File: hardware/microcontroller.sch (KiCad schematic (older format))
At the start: 13 parts, among them U6 STM32F411CEUx, Y1 12MHz

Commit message: Associate the simple parts with footprints. Some custom footprints will need to be designed.
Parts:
- C15, C21, C22, C23, C24: footprint (none) -> Capacitors_SMD:C_0603
- C16, C17, C20: footprint (none) -> Capacitors_SMD:C_0805
- C18, C19: footprint (none) -> Capacitors_SMD:C_0402
- R12: footprint (none) -> Resistors_SMD:R_0603
- U6: footprint UFQFPN48 -> Housings_DFN_QFN:QFN-48-1EP_7x7mm_Pitch0.5mm
- Y1: footprint (none) -> Crystals:Crystal_SMD_2520-4pin_2.5x2.0mm
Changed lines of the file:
@@
 F 0 "U6" H 2400 5225 50  0000 L BNN
 F 1 "STM32F411CEUx" H 9600 5225 50  0000 R BNN
-F 2 "UFQFPN48" H 9600 5175 50  0001 R TNN
+F 2 "Housings_DFN_QFN:QFN-48-1EP_7x7mm_Pitch0.5mm" H 9600 5175 50  0001 R TNN
 F 3 "" H 6000 3400 50  0001 C CNN
 	1    6000 3400
@@
 $EndComp
 $Comp
-L VDD #PWR51
+L VDD #PWR051
 U 1 1 59427B17
 P 6000 1400
-F 0 "#PWR51" H 6000 1250 50  0001 C CNN
+F 0 "#PWR051" H 6000 1250 50  0001 C CNN
 F 1 "VDD" H 6000 1550 50  0000 C CNN
 F 2 "" H 6000 1400 50  0001 C CNN
@@
 $EndComp
 $Comp
-L VDD #PWR52
+L VDD #PWR052
 U 1 1 59427B1D
 P 1850 2200
-F 0 "#PWR52" H 1850 2050 50  0001 C CNN
+F 0 "#PWR052" H 1850 2050 50  0001 C CNN
 F 1 "VDD" H 1850 2350 50  0000 C CNN
 F 2 "" H 1850 2200 50  0001 C CNN
@@
 F 0 "C17" V 1550 2350 50  0000 L CNN
 F 1 "4.7uF" V 1550 2550 50  0000 L CNN
-F 2 "" H 1500 2500 50  0001 C CNN
+F 2 "Capacitors_SMD:C_0805" H 1500 2500 50  0001 C CNN
 F 3 "" H 1500 2500 50  0001 C CNN
 	1    1500 2500
@@
 $EndComp
 $Comp
-L GND #PWR53
+L GND #PWR053
 U 1 1 59427B2A
 P 1200 2350
-F 0 "#PWR53" H 1200 2100 50  0001 C CNN
+F 0 "#PWR053" H 1200 2100 50  0001 C CNN
 F 1 "GND" V 1200 2150 50  0000 C CNN
 F 2 "" H 1200 2350 50  0001 C CNN
@@
 $EndComp
 $Comp
-L GND #PWR57
+L GND #PWR054
 U 1 1 59427B30
 P 6000 5350
-F 0 "#PWR57" H 6000 5100 50  0001 C CNN
+F 0 "#PWR054" H 6000 5100 50  0001 C CNN
 F 1 "GND" H 6000 5200 50  0000 C CNN
 F 2 "" H 6000 5350 50  0001 C CNN
@@
 F 0 "C16" V 1550 2200 50  0000 L CNN
 F 1 "1uF" V 1550 2400 50  0000 L CNN
-F 2 "" H 1500 2350 50  0001 C CNN
+F 2 "Capacitors_SMD:C_0805" H 1500 2350 50  0001 C CNN
 F 3 "" H 1500 2350 50  0001 C CNN
 	1    1500 2350
@@
 F 0 "C15" V 1550 2050 50  0000 L CNN
 F 1 "100nF" V 1550 2250 50  0000 L CNN
-F 2 "" H 1500 2200 50  0001 C CNN
+F 2 "Capacitors_SMD:C_0603" H 1500 2200 50  0001 C CNN
 F 3 "" H 1500 2200 50  0001 C CNN
 	1    1500 2200
@@
 F 0 "C21" H 4750 6550 50  0000 L CNN
 F 1 "100nF" H 4600 6750 50  0000 L CNN
-F 2 "" H 4850 6650 50  0001 C CNN
+F 2 "Capacitors_SMD:C_0603" H 4850 6650 50  0001 C CNN
 F 3 "" H 4850 6650 50  0001 C CNN
 	1    4850 6650
@@
 F 0 "C22" H 5050 6550 50  0000 L CNN
 F 1 "100nF" H 4900 6750 50  0000 L CNN
-F 2 "" H 5150 6650 50  0001 C CNN
+F 2 "Capacitors_SMD:C_0603" H 5150 6650 50  0001 C CNN
 F 3 "" H 5150 6650 50  0001 C CNN
 	1    5150 6650
@@
 F 0 "C23" H 5350 6550 50  0000 L CNN
 F 1 "100nF" H 5200 6750 50  0000 L CNN
-F 2 "" H 5450 6650 50  0001 C CNN
+F 2 "Capacitors_SMD:C_0603" H 5450 6650 50  0001 C CNN
 F 3 "" H 5450 6650 50  0001 C CNN
 	1    5450 6650
@@
 F 0 "C24" H 5650 6550 50  0000 L CNN
 F 1 "100nF" H 5500 6750 50  0000 L CNN
-F 2 "" H 5750 6650 50  0001 C CNN
+F 2 "Capacitors_SMD:C_0603" H 5750 6650 50  0001 C CNN
 F 3 "" H 5750 6650 50  0001 C CNN
 	1    5750 6650
@@
 $EndComp
 $Comp
-L GND #PWR59
+L GND #PWR055
 U 1 1 59427B60
 P 5150 6850
-F 0 "#PWR59" H 5150 6600 50  0001 C CNN
+F 0 "#PWR055" H 5150 6600 50  0001 C CNN
 F 1 "GND" H 5150 6700 50  0000 C CNN
 F 2 "" H 5150 6850 50  0001 C CNN
@@
 $EndComp
 $Comp
-L VDD #PWR58
+L VDD #PWR056
 U 1 1 59427B66
 P 5150 6450
-F 0 "#PWR58" H 5150 6300 50  0001 C CNN
+F 0 "#PWR056" H 5150 6300 50  0001 C CNN
 F 1 "VDD" H 5150 6600 50  0000 C CNN
 F 2 "" H 5150 6450 50  0001 C CNN
@@
 F 0 "C20" H 4450 6550 50  0000 L CNN
 F 1 "4.7uF" H 4300 6750 50  0000 L CNN
-F 2 "" H 4550 6650 50  0001 C CNN
+F 2 "Capacitors_SMD:C_0805" H 4550 6650 50  0001 C CNN
 F 3 "" H 4550 6650 50  0001 C CNN
 	1    4550 6650
@@
 F 0 "Y1" V 1200 2750 50  0000 L CNN
 F 1 "12MHz" V 1200 2950 50  0000 L CNN
-F 2 "" H 1350 2900 50  0001 C CNN
+F 2 "Crystals:Crystal_SMD_2520-4pin_2.5x2.0mm" H 1350 2900 50  0001 C CNN
 F 3 "" H 1350 2900 50  0001 C CNN
 	1    1350 2900
@@
 Connection ~ 1350 3100
 $Comp
-L GND #PWR55
+L GND #PWR057
 U 1 1 59427C13
 P 1150 2900
-F 0 "#PWR55" H 1150 2650 50  0001 C CNN
+F 0 "#PWR057" H 1150 2650 50  0001 C CNN
 F 1 "GND" V 1250 2850 50  0000 C CNN
 F 2 "" H 1150 2900 50  0001 C CNN
@@
 $EndComp
 $Comp
-L GND #PWR56
+L GND #PWR058
 U 1 1 59427C19
 P 1550 2900
-F 0 "#PWR56" H 1550 2650 50  0001 C CNN
+F 0 "#PWR058" H 1550 2650 50  0001 C CNN
 F 1 "GND" V 1450 2850 50  0000 C CNN
 F 2 "" H 1550 2900 50  0001 C CNN
@@
 F 0 "C19" V 1000 2950 50  0000 L CNN
 F 1 "30pF" V 1000 3150 50  0000 L CNN
-F 2 "" H 950 3100 50  0001 C CNN
+F 2 "Capacitors_SMD:C_0402" H 950 3100 50  0001 C CNN
 F 3 "" H 950 3100 50  0001 C CNN
 	1    950  3100
@@
 F 0 "C18" V 900 2550 50  0000 L CNN
 F 1 "30pF" V 900 2750 50  0000 L CNN
-F 2 "" H 950 2700 50  0001 C CNN
+F 2 "Capacitors_SMD:C_0402" H 950 2700 50  0001 C CNN
 F 3 "" H 950 2700 50  0001 C CNN
 	1    950  2700
@@
 	1050 2700 2300 2700
 $Comp
-L GND #PWR54
+L GND #PWR059
 U 1 1 59427C31
 P 800 2900
-F 0 "#PWR54" H 800 2650 50  0001 C CNN
+F 0 "#PWR059" H 800 2650 50  0001 C CNN
 F 1 "GND" V 800 2700 50  0000 C CNN
 F 2 "" H 800 2900 50  0001 C CNN
@@
 F 0 "R12" H 2130 6770 50  0000 L CNN
 F 1 "10k" H 2130 6710 50  0000 L CNN
-F 2 "" H 2100 6750 50  0001 C CNN
+F 2 "Resistors_SMD:R_0603" H 2100 6750 50  0001 C CNN
 F 3 "" H 2100 6750 50  0001 C CNN
 	1    2100 6750
@@
 $EndComp
 $Comp
-L GND #PWR60
+L GND #PWR060
 U 1 1 5942944C
 P 2100 6950
-F 0 "#PWR60" H 2100 6700 50  0001 C CNN
+F 0 "#PWR060" H 2100 6700 50  0001 C CNN
 F 1 "GND" H 2100 6800 50  0000 C CNN
 F 2 "" H 2100 6950 50  0001 C CNN

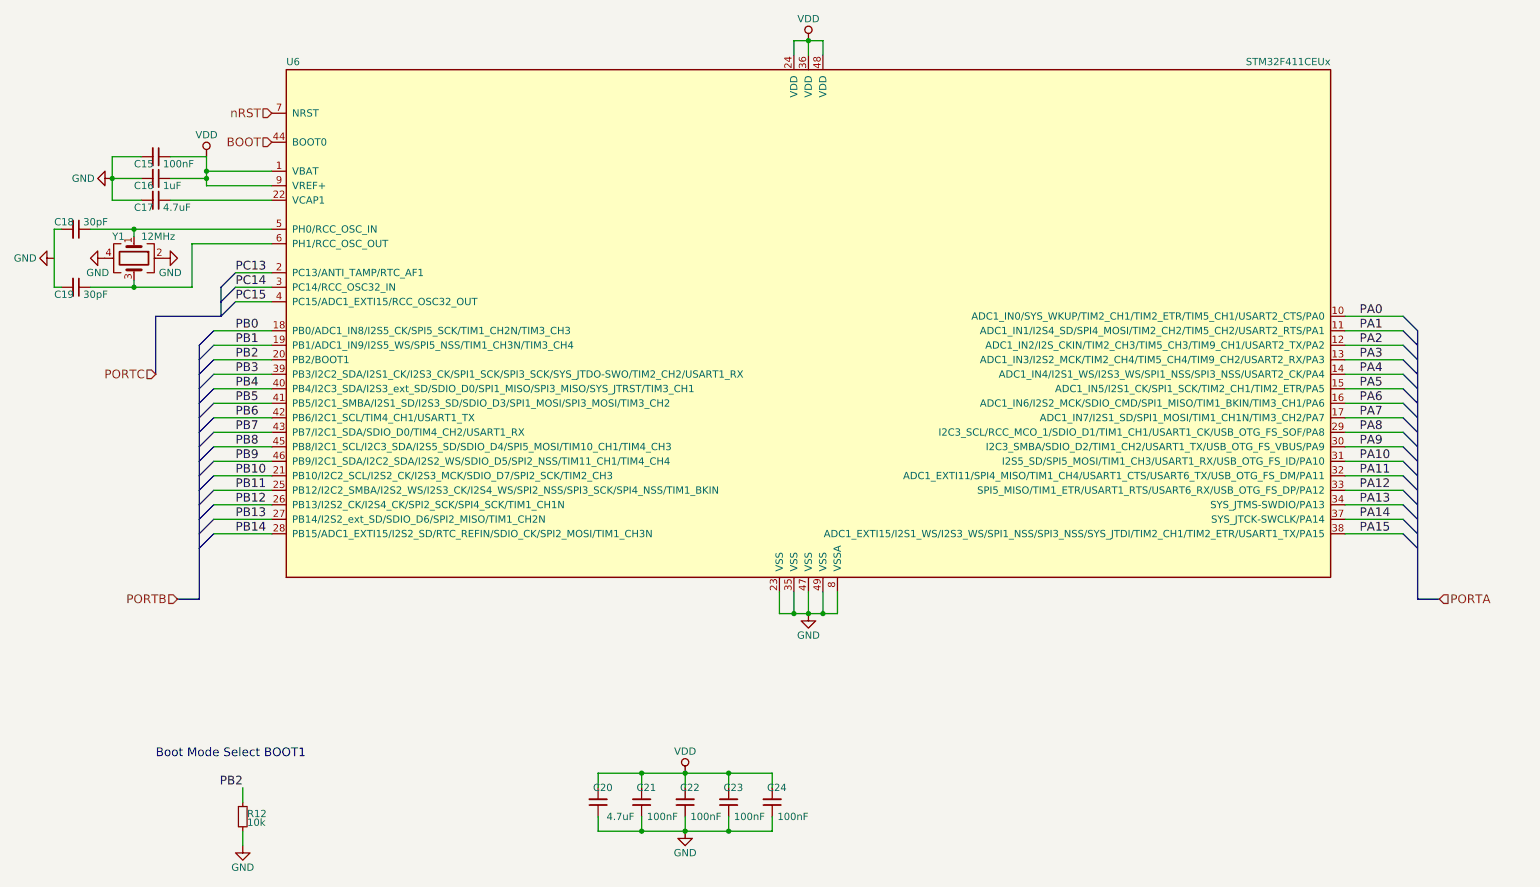
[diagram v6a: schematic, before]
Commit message: Add in some logic level translation for the camera signals. Update the annotations and plot the PDF
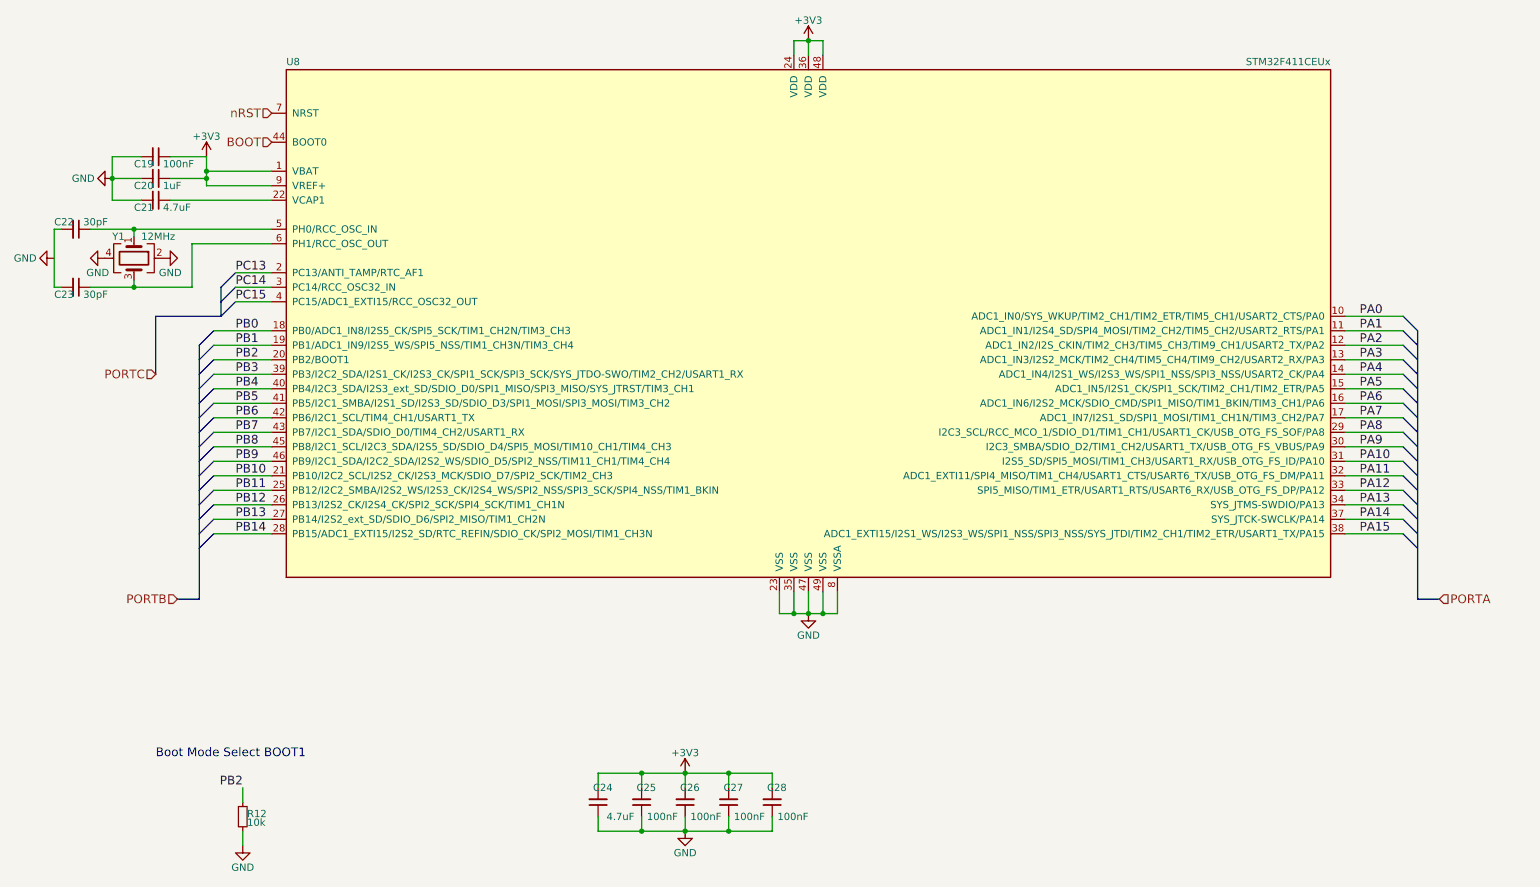
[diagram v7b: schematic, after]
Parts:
- renumbered C15 to C19, C16 to C20, C17 to C21, C18 to C22, C19 to C23, C20 to C24, C21 to C25, C22 to C26, C23 to C27, C24 to C28, U6 to U8
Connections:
- net labels added: +3V3
- net labels removed: VDD
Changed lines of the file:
@@
 P 6000 3400
 AR Path="/59427B10" Ref="U?"  Part="1"
-AR Path="/59425D39/59427B10" Ref="U6"  Part="1"
-F 0 "U6" H 2400 5225 50  0000 L BNN
+AR Path="/59425D39/59427B10" Ref="U8"  Part="1"
+F 0 "U8" H 2400 5225 50  0000 L BNN
 F 1 "STM32F411CEUx" H 9600 5225 50  0000 R BNN
 F 2 "Housings_DFN_QFN:QFN-48-1EP_7x7mm_Pitch0.5mm" H 9600 5175 50  0001 R TNN
@@
 $EndComp
 $Comp
-L VDD #PWR051
-U 1 1 59427B17
-P 6000 1400
-F 0 "#PWR051" H 6000 1250 50  0001 C CNN
-F 1 "VDD" H 6000 1550 50  0000 C CNN
-F 2 "" H 6000 1400 50  0001 C CNN
-F 3 "" H 6000 1400 50  0001 C CNN
-	1    6000 1400
-	1    0    0    -1
-$EndComp
-$Comp
-L VDD #PWR052
-U 1 1 59427B1D
-P 1850 2200
-F 0 "#PWR052" H 1850 2050 50  0001 C CNN
-F 1 "VDD" H 1850 2350 50  0000 C CNN
-F 2 "" H 1850 2200 50  0001 C CNN
-F 3 "" H 1850 2200 50  0001 C CNN
-	1    1850 2200
-	1    0    0    -1
-$EndComp
-$Comp
-L C_Small C17
+L C_Small C21
 U 1 1 59427B23
 P 1500 2500
-F 0 "C17" V 1550 2350 50  0000 L CNN
+F 0 "C21" V 1550 2350 50  0000 L CNN
 F 1 "4.7uF" V 1550 2550 50  0000 L CNN
 F 2 "Capacitors_SMD:C_0805" H 1500 2500 50  0001 C CNN
@@
 $EndComp
 $Comp
-L GND #PWR053
+L GND #PWR65
 U 1 1 59427B2A
 P 1200 2350
-F 0 "#PWR053" H 1200 2100 50  0001 C CNN
+F 0 "#PWR65" H 1200 2100 50  0001 C CNN
 F 1 "GND" V 1200 2150 50  0000 C CNN
 F 2 "" H 1200 2350 50  0001 C CNN
@@
 $EndComp
 $Comp
-L GND #PWR054
+L GND #PWR69
 U 1 1 59427B30
 P 6000 5350
-F 0 "#PWR054" H 6000 5100 50  0001 C CNN
+F 0 "#PWR69" H 6000 5100 50  0001 C CNN
 F 1 "GND" H 6000 5200 50  0000 C CNN
 F 2 "" H 6000 5350 50  0001 C CNN
@@
 $EndComp
 $Comp
-L C_Small C16
+L C_Small C20
 U 1 1 59427B36
 P 1500 2350
-F 0 "C16" V 1550 2200 50  0000 L CNN
+F 0 "C20" V 1550 2200 50  0000 L CNN
 F 1 "1uF" V 1550 2400 50  0000 L CNN
 F 2 "Capacitors_SMD:C_0805" H 1500 2350 50  0001 C CNN
@@
 $EndComp
 $Comp
-L C_Small C15
+L C_Small C19
 U 1 1 59427B3D
 P 1500 2200
-F 0 "C15" V 1550 2050 50  0000 L CNN
+F 0 "C19" V 1550 2050 50  0000 L CNN
 F 1 "100nF" V 1550 2250 50  0000 L CNN
 F 2 "Capacitors_SMD:C_0603" H 1500 2200 50  0001 C CNN
@@
 $EndComp
 $Comp
-L C_Small C21
+L C_Small C25
 U 1 1 59427B44
 P 4850 6650
-F 0 "C21" H 4750 6550 50  0000 L CNN
+F 0 "C25" H 4750 6550 50  0000 L CNN
 F 1 "100nF" H 4600 6750 50  0000 L CNN
 F 2 "Capacitors_SMD:C_0603" H 4850 6650 50  0001 C CNN
@@
 $EndComp
 $Comp
-L C_Small C22
+L C_Small C26
 U 1 1 59427B4B
 P 5150 6650
-F 0 "C22" H 5050 6550 50  0000 L CNN
+F 0 "C26" H 5050 6550 50  0000 L CNN
 F 1 "100nF" H 4900 6750 50  0000 L CNN
 F 2 "Capacitors_SMD:C_0603" H 5150 6650 50  0001 C CNN
@@
 $EndComp
 $Comp
-L C_Small C23
+L C_Small C27
 U 1 1 59427B52
 P 5450 6650
-F 0 "C23" H 5350 6550 50  0000 L CNN
+F 0 "C27" H 5350 6550 50  0000 L CNN
 F 1 "100nF" H 5200 6750 50  0000 L CNN
 F 2 "Capacitors_SMD:C_0603" H 5450 6650 50  0001 C CNN
@@
 $EndComp
 $Comp
-L C_Small C24
+L C_Small C28
 U 1 1 59427B59
 P 5750 6650
-F 0 "C24" H 5650 6550 50  0000 L CNN
+F 0 "C28" H 5650 6550 50  0000 L CNN
 F 1 "100nF" H 5500 6750 50  0000 L CNN
 F 2 "Capacitors_SMD:C_0603" H 5750 6650 50  0001 C CNN
@@
 $EndComp
 $Comp
-L GND #PWR055
+L GND #PWR71
 U 1 1 59427B60
 P 5150 6850
-F 0 "#PWR055" H 5150 6600 50  0001 C CNN
+F 0 "#PWR71" H 5150 6600 50  0001 C CNN
 F 1 "GND" H 5150 6700 50  0000 C CNN
 F 2 "" H 5150 6850 50  0001 C CNN
@@
 $EndComp
 $Comp
-L VDD #PWR056
-U 1 1 59427B66
-P 5150 6450
-F 0 "#PWR056" H 5150 6300 50  0001 C CNN
-F 1 "VDD" H 5150 6600 50  0000 C CNN
-F 2 "" H 5150 6450 50  0001 C CNN
-F 3 "" H 5150 6450 50  0001 C CNN
-	1    5150 6450
-	1    0    0    -1
-$EndComp
-$Comp
-L C_Small C20
+L C_Small C24
 U 1 1 59427B6C
 P 4550 6650
-F 0 "C20" H 4450 6550 50  0000 L CNN
+F 0 "C24" H 4450 6550 50  0000 L CNN
 F 1 "4.7uF" H 4300 6750 50  0000 L CNN
 F 2 "Capacitors_SMD:C_0805" H 4550 6650 50  0001 C CNN
@@
 Connection ~ 1350 3100
 $Comp
-L GND #PWR057
+L GND #PWR67
 U 1 1 59427C13
 P 1150 2900
-F 0 "#PWR057" H 1150 2650 50  0001 C CNN
+F 0 "#PWR67" H 1150 2650 50  0001 C CNN
 F 1 "GND" V 1250 2850 50  0000 C CNN
 F 2 "" H 1150 2900 50  0001 C CNN
@@
 $EndComp
 $Comp
-L GND #PWR058
+L GND #PWR68
 U 1 1 59427C19
 P 1550 2900
-F 0 "#PWR058" H 1550 2650 50  0001 C CNN
+F 0 "#PWR68" H 1550 2650 50  0001 C CNN
 F 1 "GND" V 1450 2850 50  0000 C CNN
 F 2 "" H 1550 2900 50  0001 C CNN
@@
 $EndComp
 $Comp
-L C_Small C19
+L C_Small C23
 U 1 1 59427C1F
 P 950 3100
-F 0 "C19" V 1000 2950 50  0000 L CNN
+F 0 "C23" V 1000 2950 50  0000 L CNN
 F 1 "30pF" V 1000 3150 50  0000 L CNN
 F 2 "Capacitors_SMD:C_0402" H 950 3100 50  0001 C CNN
@@
 	1750 3100 1050 3100
 $Comp
-L C_Small C18
+L C_Small C22
 U 1 1 59427C28
 P 950 2700
-F 0 "C18" V 900 2550 50  0000 L CNN
+F 0 "C22" V 900 2550 50  0000 L CNN
 F 1 "30pF" V 900 2750 50  0000 L CNN
 F 2 "Capacitors_SMD:C_0402" H 950 2700 50  0001 C CNN
@@
 	1050 2700 2300 2700
 $Comp
-L GND #PWR059
+L GND #PWR66
 U 1 1 59427C31
 P 800 2900
-F 0 "#PWR059" H 800 2650 50  0001 C CNN
+F 0 "#PWR66" H 800 2650 50  0001 C CNN
 F 1 "GND" V 800 2700 50  0000 C CNN
 F 2 "" H 800 2900 50  0001 C CNN
@@
 $EndComp
 $Comp
-L GND #PWR060
+L GND #PWR72
 U 1 1 5942944C
 P 2100 6950
-F 0 "#PWR060" H 2100 6700 50  0001 C CNN
+F 0 "#PWR72" H 2100 6700 50  0001 C CNN
 F 1 "GND" H 2100 6800 50  0000 C CNN
 F 2 "" H 2100 6950 50  0001 C CNN
@@
 Text HLabel 1500 3700 0    60   Input ~ 0
 PORTC
+$Comp
+L +3V3 #PWR63
+U 1 1 59492047
+P 6000 1400
+F 0 "#PWR63" H 6000 1250 50  0001 C CNN
+F 1 "+3V3" H 6000 1540 50  0000 C CNN
+F 2 "" H 6000 1400 50  0001 C CNN
+F 3 "" H 6000 1400 50  0001 C CNN
+	1    6000 1400
+	1    0    0    -1
+$EndComp
+$Comp
+L +3V3 #PWR70
+U 1 1 59492080
+P 5150 6450
+F 0 "#PWR70" H 5150 6300 50  0001 C CNN
+F 1 "+3V3" H 5150 6590 50  0000 C CNN
+F 2 "" H 5150 6450 50  0001 C CNN
+F 3 "" H 5150 6450 50  0001 C CNN
+	1    5150 6450
+	1    0    0    -1
+$EndComp
+$Comp
+L +3V3 #PWR64
+U 1 1 594920B2
+P 1850 2200
+F 0 "#PWR64" H 1850 2050 50  0001 C CNN
+F 1 "+3V3" H 1850 2340 50  0000 C CNN
+F 2 "" H 1850 2200 50  0001 C CNN
+F 3 "" H 1850 2200 50  0001 C CNN
+	1    1850 2200
+	1    0    0    -1
+$EndComp
 $EndSCHEMATC
